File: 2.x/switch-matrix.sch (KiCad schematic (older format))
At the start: 32 parts, among them P6 HE10-32, Q25 BC846, Q26 BC846, Q27 BC846, Q28 BC846, U1 74LVC14

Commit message: Cleaning up schematic Updating solenoid driver to use 12V for MOSFET gates instead of Vsol so we never exceed Vgs_max
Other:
- moved on the sheet: P6

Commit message: Started layout on 2.0
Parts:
- C2: renamed from C3; footprint ~ -> Capacitors_SMD:C_0603
- C3: renamed from C2; footprint ~ -> Capacitors_SMD:C_0805
- D25, D26, D27, D28, D29, D30, D31, D32: value DOUBLE_SCH_KCOM -> BAT54C; footprint ~ -> Housings_SOT-23_SOT-143_TSOT-6:SOT-23
- P6: footprint (none) -> Pin_Headers:Pin_Header_Straight_2x16
- Q25, Q26, Q27, Q28: footprint SOT-23 -> Housings_SOT-23_SOT-143_TSOT-6:SOT-23
- R100: renamed from R88; footprint ~ -> Resistors_SMD:R_0603
- R85: renamed from R89; footprint ~ -> Resistors_SMD:R_0603
- R86: renamed from R90; footprint ~ -> Resistors_SMD:R_0603
- R87: renamed from R91; footprint ~ -> Resistors_SMD:R_0603
- R88: renamed from R92; footprint ~ -> Resistors_SMD:R_0603
- R89: renamed from R93; footprint ~ -> Resistors_SMD:R_0603
- R90: renamed from R94; footprint ~ -> Resistors_SMD:R_0603
- R91: renamed from R85; footprint ~ -> Resistors_SMD:R_0603
- R92: renamed from R95; footprint ~ -> Resistors_SMD:R_0603
- R93: renamed from R86; footprint ~ -> Resistors_SMD:R_0603
- R94: renamed from R96; footprint ~ -> Resistors_SMD:R_0603
- R95: renamed from R87; footprint ~ -> Resistors_SMD:R_0603
- R96: renamed from R97; footprint ~ -> Resistors_SMD:R_0603
- R97: renamed from R98; footprint ~ -> Resistors_SMD:R_0603
- R98: renamed from R99; footprint ~ -> Resistors_SMD:R_0603
- R99: renamed from R100; footprint ~ -> Resistors_SMD:R_0603
- U1: footprint ~ -> Housings_SSOP:SSOP-14_5.3x6.2mm_Pitch0.65mm
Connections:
- net labels added: SWITCH_12V
- net labels removed: SWITCH_PWR

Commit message: 100% routed.
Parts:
- removed D25, D26, D27, D28, D29, D30, D31, D32: BAT54C, Housings_SOT-23_SOT-143_TSOT-6:SOT-23, symbol DOUBLE_SCH_KCOM
- added D25, D26, D27, D28, D29, D30, D31, D32: BAT54C, symbol BAT54C
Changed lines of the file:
@@
 Text Label 10350 4200 2    60   ~ 0
 COL3_SWITCHED
-$Comp
-L DOUBLE_SCH_KCOM D32
-U 1 1 53156145
-P 7350 5500
-F 0 "D32" H 7500 5375 60  0000 C CNN
-F 1 "BAT54C" H 7350 5650 60  0000 C CNN
-F 2 "Housings_SOT-23_SOT-143_TSOT-6:SOT-23" H 7350 5500 60  0001 C CNN
-F 3 "~" H 7350 5500 60  0000 C CNN
-	1    7350 5500
-	1    0    0    -1
-$EndComp
-$Comp
-L DOUBLE_SCH_KCOM D31
-U 1 1 53156154
-P 6450 5500
-F 0 "D31" H 6600 5375 60  0000 C CNN
-F 1 "BAT54C" H 6450 5650 60  0000 C CNN
-F 2 "Housings_SOT-23_SOT-143_TSOT-6:SOT-23" H 6450 5500 60  0001 C CNN
-F 3 "~" H 6450 5500 60  0000 C CNN
-	1    6450 5500
-	1    0    0    -1
-$EndComp
-$Comp
-L DOUBLE_SCH_KCOM D30
-U 1 1 531564D4
-P 5550 5500
-F 0 "D30" H 5700 5375 60  0000 C CNN
-F 1 "BAT54C" H 5550 5650 60  0000 C CNN
-F 2 "Housings_SOT-23_SOT-143_TSOT-6:SOT-23" H 5550 5500 60  0001 C CNN
-F 3 "~" H 5550 5500 60  0000 C CNN
-	1    5550 5500
-	1    0    0    -1
-$EndComp
-$Comp
-L DOUBLE_SCH_KCOM D29
-U 1 1 531564E3
-P 4650 5500
-F 0 "D29" H 4800 5375 60  0000 C CNN
-F 1 "BAT54C" H 4650 5650 60  0000 C CNN
-F 2 "Housings_SOT-23_SOT-143_TSOT-6:SOT-23" H 4650 5500 60  0001 C CNN
-F 3 "~" H 4650 5500 60  0000 C CNN
-	1    4650 5500
-	1    0    0    -1
-$EndComp
-$Comp
-L DOUBLE_SCH_KCOM D28
-U 1 1 531564F2
-P 3750 5500
-F 0 "D28" H 3900 5375 60  0000 C CNN
-F 1 "BAT54C" H 3750 5650 60  0000 C CNN
-F 2 "Housings_SOT-23_SOT-143_TSOT-6:SOT-23" H 3750 5500 60  0001 C CNN
-F 3 "~" H 3750 5500 60  0000 C CNN
-	1    3750 5500
-	1    0    0    -1
-$EndComp
-$Comp
-L DOUBLE_SCH_KCOM D27
-U 1 1 53156501
-P 2850 5500
-F 0 "D27" H 3000 5375 60  0000 C CNN
-F 1 "BAT54C" H 2850 5650 60  0000 C CNN
-F 2 "Housings_SOT-23_SOT-143_TSOT-6:SOT-23" H 2850 5500 60  0001 C CNN
-F 3 "~" H 2850 5500 60  0000 C CNN
-	1    2850 5500
-	1    0    0    -1
-$EndComp
-$Comp
-L DOUBLE_SCH_KCOM D26
-U 1 1 53156510
-P 1950 5500
-F 0 "D26" H 2100 5375 60  0000 C CNN
-F 1 "BAT54C" H 1950 5650 60  0000 C CNN
-F 2 "Housings_SOT-23_SOT-143_TSOT-6:SOT-23" H 1950 5500 60  0001 C CNN
-F 3 "~" H 1950 5500 60  0000 C CNN
-	1    1950 5500
-	1    0    0    -1
-$EndComp
-$Comp
-L DOUBLE_SCH_KCOM D25
-U 1 1 5315651F
-P 1050 5500
-F 0 "D25" H 1200 5375 60  0000 C CNN
-F 1 "BAT54C" H 1050 5650 60  0000 C CNN
-F 2 "Housings_SOT-23_SOT-143_TSOT-6:SOT-23" H 1050 5500 60  0001 C CNN
-F 3 "~" H 1050 5500 60  0000 C CNN
-	1    1050 5500
-	1    0    0    -1
-$EndComp
 Text Label 8300 5800 2    60   ~ 0
 ROW3_SWITCHED
@@
 Wire Wire Line
 	7750 5400 7750 5500
+$Comp
+L BAT54C D25
+U 1 1 55709451
+P 1050 5500
+F 0 "D25" H 1200 5375 60  0000 C CNN
+F 1 "BAT54C" H 1050 5650 60  0000 C CNN
+F 2 "" H 1050 5500 60  0000 C CNN
+F 3 "" H 1050 5500 60  0000 C CNN
+	1    1050 5500
+	1    0    0    -1
+$EndComp
+$Comp
+L BAT54C D26
+U 1 1 557098BF
+P 1950 5500
+F 0 "D26" H 2100 5375 60  0000 C CNN
+F 1 "BAT54C" H 1950 5650 60  0000 C CNN
+F 2 "" H 1950 5500 60  0000 C CNN
+F 3 "" H 1950 5500 60  0000 C CNN
+	1    1950 5500
+	1    0    0    -1
+$EndComp
+$Comp
+L BAT54C D27
+U 1 1 5570A36E
+P 2850 5500
+F 0 "D27" H 3000 5375 60  0000 C CNN
+F 1 "BAT54C" H 2850 5650 60  0000 C CNN
+F 2 "" H 2850 5500 60  0000 C CNN
+F 3 "" H 2850 5500 60  0000 C CNN
+	1    2850 5500
+	1    0    0    -1
+$EndComp
+$Comp
+L BAT54C D28
+U 1 1 5570A3BE
+P 3750 5500
+F 0 "D28" H 3900 5375 60  0000 C CNN
+F 1 "BAT54C" H 3750 5650 60  0000 C CNN
+F 2 "" H 3750 5500 60  0000 C CNN
+F 3 "" H 3750 5500 60  0000 C CNN
+	1    3750 5500
+	1    0    0    -1
+$EndComp
+$Comp
+L BAT54C D29
+U 1 1 5570AB55
+P 4650 5500
+F 0 "D29" H 4800 5375 60  0000 C CNN
+F 1 "BAT54C" H 4650 5650 60  0000 C CNN
+F 2 "" H 4650 5500 60  0000 C CNN
+F 3 "" H 4650 5500 60  0000 C CNN
+	1    4650 5500
+	1    0    0    -1
+$EndComp
+$Comp
+L BAT54C D30
+U 1 1 5570ABA5
+P 5550 5500
+F 0 "D30" H 5700 5375 60  0000 C CNN
+F 1 "BAT54C" H 5550 5650 60  0000 C CNN
+F 2 "" H 5550 5500 60  0000 C CNN
+F 3 "" H 5550 5500 60  0000 C CNN
+	1    5550 5500
+	1    0    0    -1
+$EndComp
+$Comp
+L BAT54C D31
+U 1 1 5570AD93
+P 6450 5500
+F 0 "D31" H 6600 5375 60  0000 C CNN
+F 1 "BAT54C" H 6450 5650 60  0000 C CNN
+F 2 "" H 6450 5500 60  0000 C CNN
+F 3 "" H 6450 5500 60  0000 C CNN
+	1    6450 5500
+	1    0    0    -1
+$EndComp
+$Comp
+L BAT54C D32
+U 1 1 5570AEF2
+P 7350 5500
+F 0 "D32" H 7500 5375 60  0000 C CNN
+F 1 "BAT54C" H 7350 5650 60  0000 C CNN
+F 2 "" H 7350 5500 60  0000 C CNN
+F 3 "" H 7350 5500 60  0000 C CNN
+	1    7350 5500
+	1    0    0    -1
+$EndComp
 $EndSCHEMATC

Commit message: Fixing BAT54C pinout, and some feedback from layout review.
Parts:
- D25, D26, D27, D28, D29, D30, D31, D32: footprint (none) -> Housings_SOT-23_SOT-143_TSOT-6:SOT-23
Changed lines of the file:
@@
 F 0 "D25" H 1200 5375 60  0000 C CNN
 F 1 "BAT54C" H 1050 5650 60  0000 C CNN
-F 2 "" H 1050 5500 60  0000 C CNN
+F 2 "Housings_SOT-23_SOT-143_TSOT-6:SOT-23" H 1050 5500 60  0001 C CNN
 F 3 "" H 1050 5500 60  0000 C CNN
 	1    1050 5500
@@
 F 0 "D26" H 2100 5375 60  0000 C CNN
 F 1 "BAT54C" H 1950 5650 60  0000 C CNN
-F 2 "" H 1950 5500 60  0000 C CNN
+F 2 "Housings_SOT-23_SOT-143_TSOT-6:SOT-23" H 1950 5500 60  0001 C CNN
 F 3 "" H 1950 5500 60  0000 C CNN
 	1    1950 5500
@@
 F 0 "D27" H 3000 5375 60  0000 C CNN
 F 1 "BAT54C" H 2850 5650 60  0000 C CNN
-F 2 "" H 2850 5500 60  0000 C CNN
+F 2 "Housings_SOT-23_SOT-143_TSOT-6:SOT-23" H 2850 5500 60  0001 C CNN
 F 3 "" H 2850 5500 60  0000 C CNN
 	1    2850 5500
@@
 F 0 "D28" H 3900 5375 60  0000 C CNN
 F 1 "BAT54C" H 3750 5650 60  0000 C CNN
-F 2 "" H 3750 5500 60  0000 C CNN
+F 2 "Housings_SOT-23_SOT-143_TSOT-6:SOT-23" H 3750 5500 60  0001 C CNN
 F 3 "" H 3750 5500 60  0000 C CNN
 	1    3750 5500
@@
 F 0 "D29" H 4800 5375 60  0000 C CNN
 F 1 "BAT54C" H 4650 5650 60  0000 C CNN
-F 2 "" H 4650 5500 60  0000 C CNN
+F 2 "Housings_SOT-23_SOT-143_TSOT-6:SOT-23" H 4650 5500 60  0001 C CNN
 F 3 "" H 4650 5500 60  0000 C CNN
 	1    4650 5500
@@
 F 0 "D30" H 5700 5375 60  0000 C CNN
 F 1 "BAT54C" H 5550 5650 60  0000 C CNN
-F 2 "" H 5550 5500 60  0000 C CNN
+F 2 "Housings_SOT-23_SOT-143_TSOT-6:SOT-23" H 5550 5500 60  0001 C CNN
 F 3 "" H 5550 5500 60  0000 C CNN
 	1    5550 5500
@@
 F 0 "D31" H 6600 5375 60  0000 C CNN
 F 1 "BAT54C" H 6450 5650 60  0000 C CNN
-F 2 "" H 6450 5500 60  0000 C CNN
+F 2 "Housings_SOT-23_SOT-143_TSOT-6:SOT-23" H 6450 5500 60  0001 C CNN
 F 3 "" H 6450 5500 60  0000 C CNN
 	1    6450 5500
@@
 F 0 "D32" H 7500 5375 60  0000 C CNN
 F 1 "BAT54C" H 7350 5650 60  0000 C CNN
-F 2 "" H 7350 5500 60  0000 C CNN
+F 2 "Housings_SOT-23_SOT-143_TSOT-6:SOT-23" H 7350 5500 60  0001 C CNN
 F 3 "" H 7350 5500 60  0000 C CNN
 	1    7350 5500

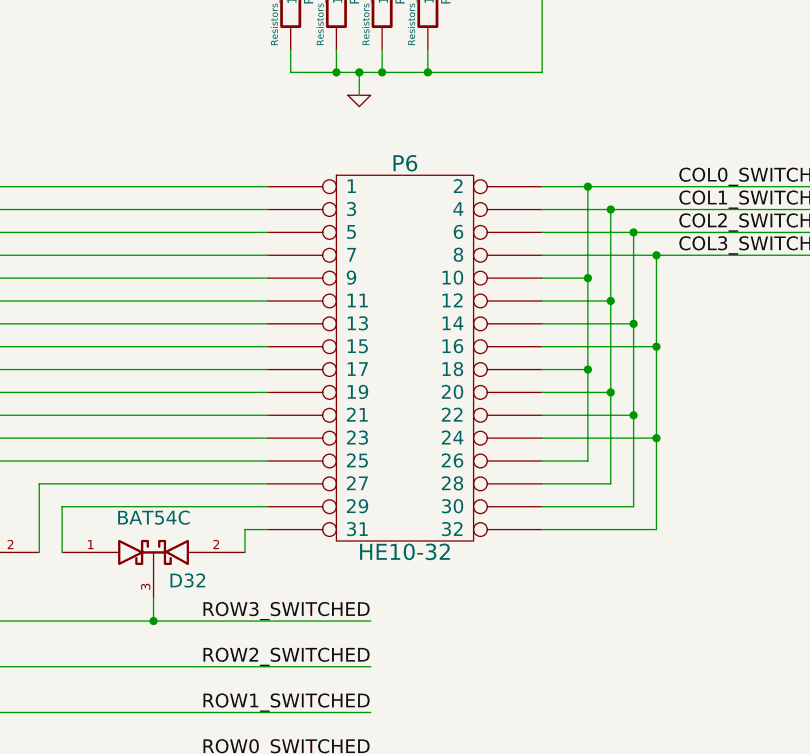
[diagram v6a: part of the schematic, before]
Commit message: Updated solenoid driver with new resistor arrangement, and changed footprint on switch matrix to a connector we can actually get.
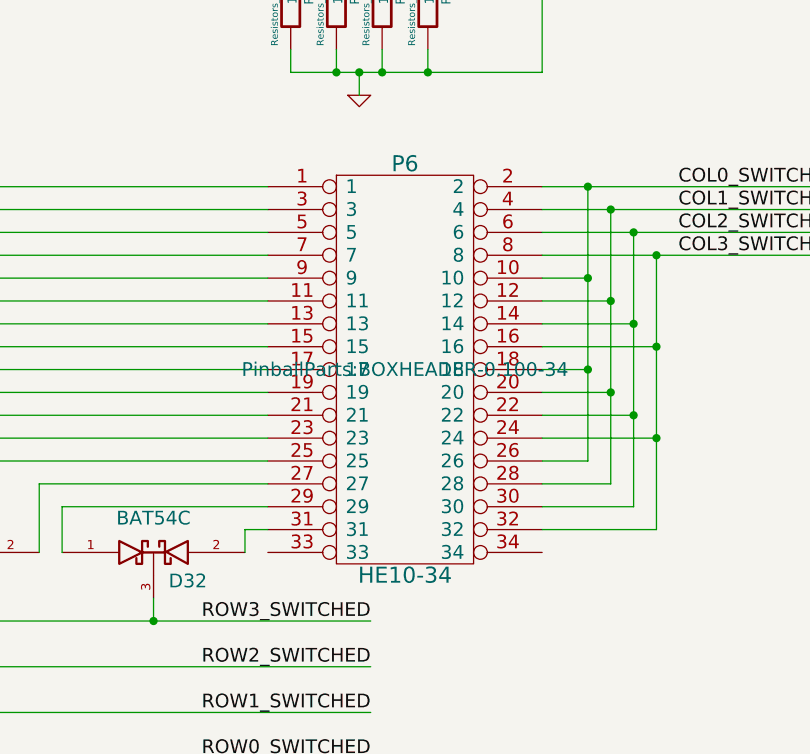
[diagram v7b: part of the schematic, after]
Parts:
- removed P6: HE10-32, Pin_Headers:Pin_Header_Straight_2x16, symbol HE10-32
- added P6: HE10-34, PinballParts:BOXHEADER-0.100-34, symbol HE10-34
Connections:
- net COL0_SWITCHED: now also P6.10, P6.18, P6.2, P6.26
- net COL1_SWITCHED: now also P6.12, P6.20, P6.28, P6.4
- net COL2_SWITCHED: now also P6.14, P6.22, P6.30, P6.6
- net COL3_SWITCHED: now also P6.16, P6.24, P6.32, P6.8
- net at D25.1 (Anode): now also P6.1
- net at D27.2 (cathode): now also P6.11
- net at D28.1 (Anode): now also P6.13
- net at D28.2 (cathode): now also P6.15
- net at D29.1 (Anode): now also P6.17
- net at D29.2 (cathode): now also P6.19
- net at D30.1 (Anode): now also P6.21
- net at D30.2 (cathode): now also P6.23
- net at D31.1 (Anode): now also P6.25
- net at D31.2 (cathode): now also P6.27
- net at D32.1 (Anode): now also P6.29
- net at D25.2 (cathode): now also P6.3
- net at D32.2 (cathode): now also P6.31
- net at D26.1 (Anode): now also P6.5
- net at D26.2 (cathode): now also P6.7
- net at D27.1 (Anode): now also P6.9
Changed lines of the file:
@@
 Text Label 6450 2700 0    60   ~ 0
 ROW3_SWITCHED
-$Comp
-L HE10-32 P6
-U 1 1 53155A3D
-P 8450 4650
-F 0 "P6" H 8450 5500 70  0000 C CNN
-F 1 "HE10-32" H 8450 3800 70  0000 C CNN
-F 2 "Pin_Headers:Pin_Header_Straight_2x16" H 8450 4650 60  0001 C CNN
-F 3 "" H 8450 4650 60  0000 C CNN
-	1    8450 4650
-	1    0    0    -1
-$EndComp
 Text Label 10350 3900 2    60   ~ 0
 COL0_SWITCHED
@@
 	1    0    0    -1
 $EndComp
+$Comp
+L HE10-34 P6
+U 1 1 557F0C76
+P 8450 4700
+F 0 "P6" H 8450 5600 70  0000 C CNN
+F 1 "HE10-34" H 8450 3800 70  0000 C CNN
+F 2 "PinballParts:BOXHEADER-0.100-34" H 8450 4700 60  0000 C CNN
+F 3 "" H 8450 4700 60  0000 C CNN
+	1    8450 4700
+	1    0    0    -1
+$EndComp

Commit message: Committing latest files. This includes the KiCAD 4.0.0rc1 migration as well as the updates to Base Board 2.1.
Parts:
- C2: symbol C -> C-RESCUE-base-module-hardware-v2
- C3: symbol CP -> CP-RESCUE-base-module-hardware-v2
- R100, R85, R86, R87, R88, R89, R90, R91, R92, R93, R94, R95, R96, R97, R98, R99: symbol R -> R-RESCUE-base-module-hardware-v2
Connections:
- net GND: now also P6.33
- net SWITCH_12V: now also P6.34
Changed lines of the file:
@@
 EESchema Schematic File Version 2
+LIBS:base-module-hardware-v2-rescue
 LIBS:power
 LIBS:device
@@
 LIBS:memory
 LIBS:xilinx
-LIBS:special
 LIBS:microcontrollers
 LIBS:dsp
@@
 COL3
 $Comp
-L R R91
+L R-RESCUE-base-module-hardware-v2 R91
 U 1 1 53150FDD
 P 2150 2300
@@
 $EndComp
 $Comp
-L R R93
+L R-RESCUE-base-module-hardware-v2 R93
 U 1 1 53150FED
 P 2150 2600
@@
 $EndComp
 $Comp
-L R R95
+L R-RESCUE-base-module-hardware-v2 R95
 U 1 1 53150FFD
 P 2150 2900
@@
 $EndComp
 $Comp
-L R R100
+L R-RESCUE-base-module-hardware-v2 R100
 U 1 1 53151003
 P 2150 3200
@@
 $EndComp
 $Comp
-L R R88
+L R-RESCUE-base-module-hardware-v2 R88
 U 1 1 53151087
 P 4800 1650
@@
 $EndComp
 $Comp
-L R R87
+L R-RESCUE-base-module-hardware-v2 R87
 U 1 1 5315108D
 P 4400 1650
@@
 $EndComp
 $Comp
-L R R86
+L R-RESCUE-base-module-hardware-v2 R86
 U 1 1 53151093
 P 4000 1650
@@
 $EndComp
 $Comp
-L R R85
+L R-RESCUE-base-module-hardware-v2 R85
 U 1 1 53151099
 P 3600 1650
@@
 COL3_SWITCHED
 $Comp
-L R R89
+L R-RESCUE-base-module-hardware-v2 R89
 U 1 1 531513F9
 P 7600 1800
@@
 $EndComp
 $Comp
-L R R90
+L R-RESCUE-base-module-hardware-v2 R90
 U 1 1 531513FF
 P 7600 2100
@@
 $EndComp
 $Comp
-L R R92
+L R-RESCUE-base-module-hardware-v2 R92
 U 1 1 53151405
 P 7600 2400
@@
 $EndComp
 $Comp
-L R R94
+L R-RESCUE-base-module-hardware-v2 R94
 U 1 1 5315140B
 P 7600 2700
@@
 $EndComp
 $Comp
-L R R96
+L R-RESCUE-base-module-hardware-v2 R96
 U 1 1 53151411
 P 7950 3050
@@
 $EndComp
 $Comp
-L R R97
+L R-RESCUE-base-module-hardware-v2 R97
 U 1 1 53151417
 P 8150 3050
@@
 $EndComp
 $Comp
-L R R98
+L R-RESCUE-base-module-hardware-v2 R98
 U 1 1 5315141D
 P 8350 3050
@@
 $EndComp
 $Comp
-L R R99
+L R-RESCUE-base-module-hardware-v2 R99
 U 1 1 53151423
 P 8550 3050
@@
 	9050 1150 9050 1700
 Wire Wire Line
-	1200 950  4200 950
+	1200 950  10400 950
 Connection ~ 4200 1300
 Wire Wire Line
 	4200 950  4200 1300
 $Comp
-L GND #PWR023
+L GND-RESCUE-base-module-hardware-v2 #PWR023
 U 1 1 5315785A
 P 4200 3600
@@
 $EndComp
 $Comp
-L GND #PWR024
+L GND-RESCUE-base-module-hardware-v2 #PWR024
 U 1 1 53157869
 P 8250 3500
@@
 Connection ~ 8550 3400
 $Comp
-L C C2
+L C-RESCUE-base-module-hardware-v2 C2
 U 1 1 53157E8B
 P 9350 1350
@@
 $EndComp
 $Comp
-L GND #PWR025
+L GND-RESCUE-base-module-hardware-v2 #PWR025
 U 1 1 53157E9F
 P 9350 1550
@@
 Connection ~ 9050 1150
 $Comp
-L CP C3
+L CP-RESCUE-base-module-hardware-v2 C3
 U 1 1 5315801F
 P 1600 1450
@@
 $EndComp
 $Comp
-L GND #PWR026
+L GND-RESCUE-base-module-hardware-v2 #PWR026
 U 1 1 53158033
 P 1600 1750
@@
 	1    0    0    -1
 $EndComp
+$Comp
+L GND-RESCUE-base-module-hardware-v2 #PWR?
+U 1 1 561208A7
+P 7800 5600
+F 0 "#PWR?" H 7800 5600 30  0001 C CNN
+F 1 "GND-RESCUE-base-module-hardware-v2" H 7800 5530 30  0001 C CNN
+F 2 "" H 7800 5600 60  0000 C CNN
+F 3 "" H 7800 5600 60  0000 C CNN
+	1    7800 5600
+	1    0    0    -1
+$EndComp
+Wire Wire Line
+	7850 5500 7800 5500
+Wire Wire Line
+	7800 5500 7800 5600
+Wire Wire Line
+	10400 950  10400 5500
+Wire Wire Line
+	10400 5500 9050 5500
+Connection ~ 4200 950
 $EndSCHEMATC
